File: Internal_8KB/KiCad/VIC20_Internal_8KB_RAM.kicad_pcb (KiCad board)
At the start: 2 copper layers, 70 x 60 mm, 10 parts, among them J1 UD4, J2 UE4, J3 SW, J4 Signals, U1 6264, U2 GAL16V8

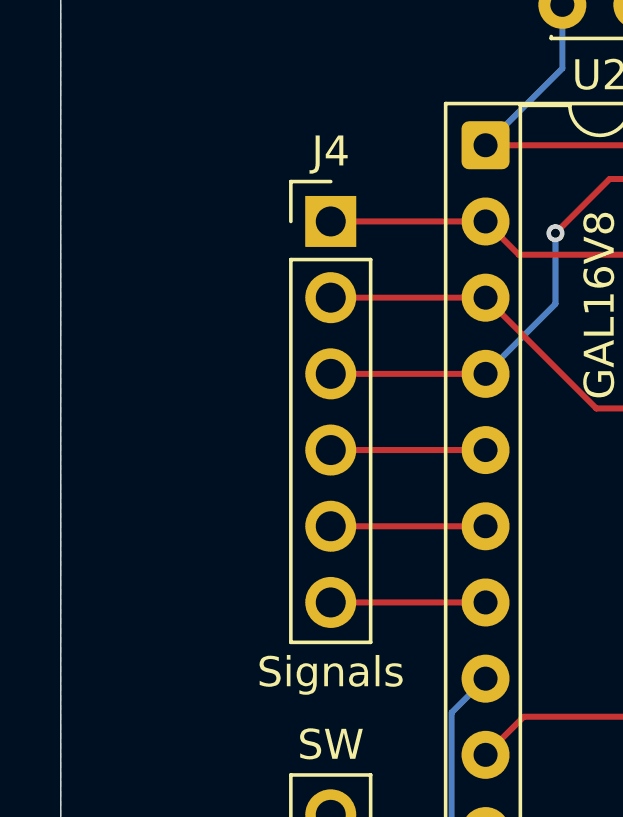
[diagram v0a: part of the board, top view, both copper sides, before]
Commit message: Added pin naming
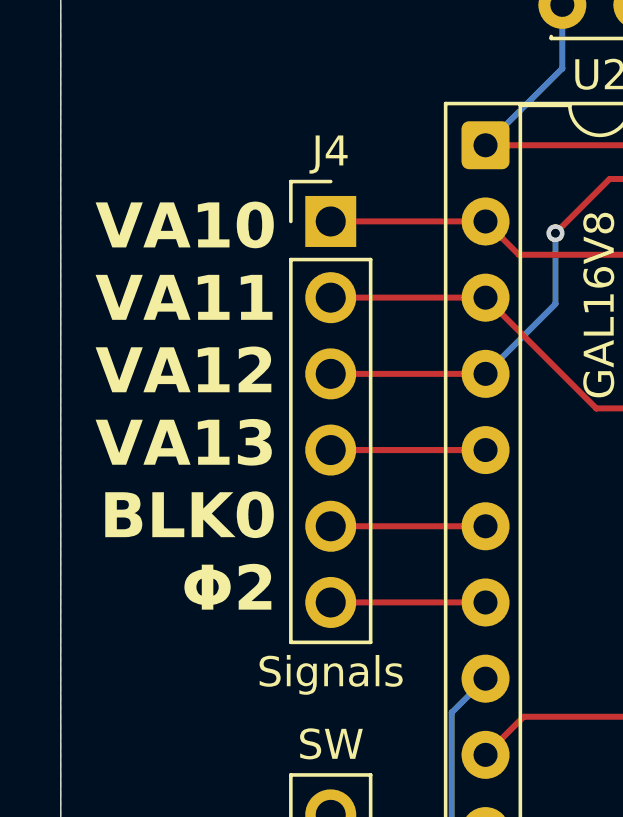
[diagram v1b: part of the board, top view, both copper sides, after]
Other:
- board text added: "VA10 VA11 VA12 VA13 BLK0 Φ2"
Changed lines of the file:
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@@
+		)
+	)
+	(gr_text "VA10\nVA11\nVA12\nVA13\nBLK0\nΦ2"
+		(at 152.68 96.862974 0)
+		(layer "F.SilkS")
+		(effects
+			(font
+				(size 1.5 1.5)
+				(thickness 0.3)
+				(bold yes)
+			)
+			(justify right bottom)
 		)
 	)

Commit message: Cosmetic updates to schematic
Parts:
- moved U1 100.8 mm to (97.4, 47.6)
- moved G*** 100.8 mm to (63.0, 38.1)
- moved J3 100.8 mm to (58.0, 76.7)
- moved C1 100.8 mm to (106.3, 42.7)
- moved C2 100.8 mm to (65.8, 47.1)
- moved J1 100.8 mm to (80.0, 36.1)
- moved J2 100.8 mm to (80.0, 66.1)
- moved J4 100.8 mm to (58.0, 54.3)
- moved R1 100.8 mm to (70.6, 78.1)
- moved U2 100.8 mm to (63.2, 51.8)
